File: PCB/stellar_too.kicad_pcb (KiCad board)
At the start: 2 copper layers, 139 x 121 mm, 61 parts, among them J1 USB_C_Receptacle_USB2.0_14P, J2 USB_C_Receptacle_USB2.0_16P, SW1 SW_Push_45deg, SW10 SW_Push_45deg, SW11 SW_Push_45deg, SW12 SW_Push_45deg, SW13 SW_Push_45deg, SW14 SW_Push_45deg, SW15 SW_Push_45deg, SW16 SW_Push_45deg, SW17 SW_Push_45deg, SW18 SW_Push_45deg, SW19 SW_Push_45deg, SW2 SW_Push_45deg, SW20 SW_Push_45deg, SW21 SW_Push_45deg, SW22 SW_Push_45deg, SW23 SW_Push_45deg, SW24 SW_Push_45deg, SW25 SW_Push_45deg, SW26 SW_Push_45deg, SW27 SW_Push_45deg, SW28 SW_Push_45deg, SW3 SW_Push_45deg, SW4 SW_Push_45deg, SW5 SW_Push_45deg, SW6 SW_Push_45deg, SW7 SW_Push_45deg, SW8 SW_Push_45deg, SW9 SW_Push_45deg, U1 MDBT50Q, U2 FUSB302B01MPX, U3 FUSB302B01MPX

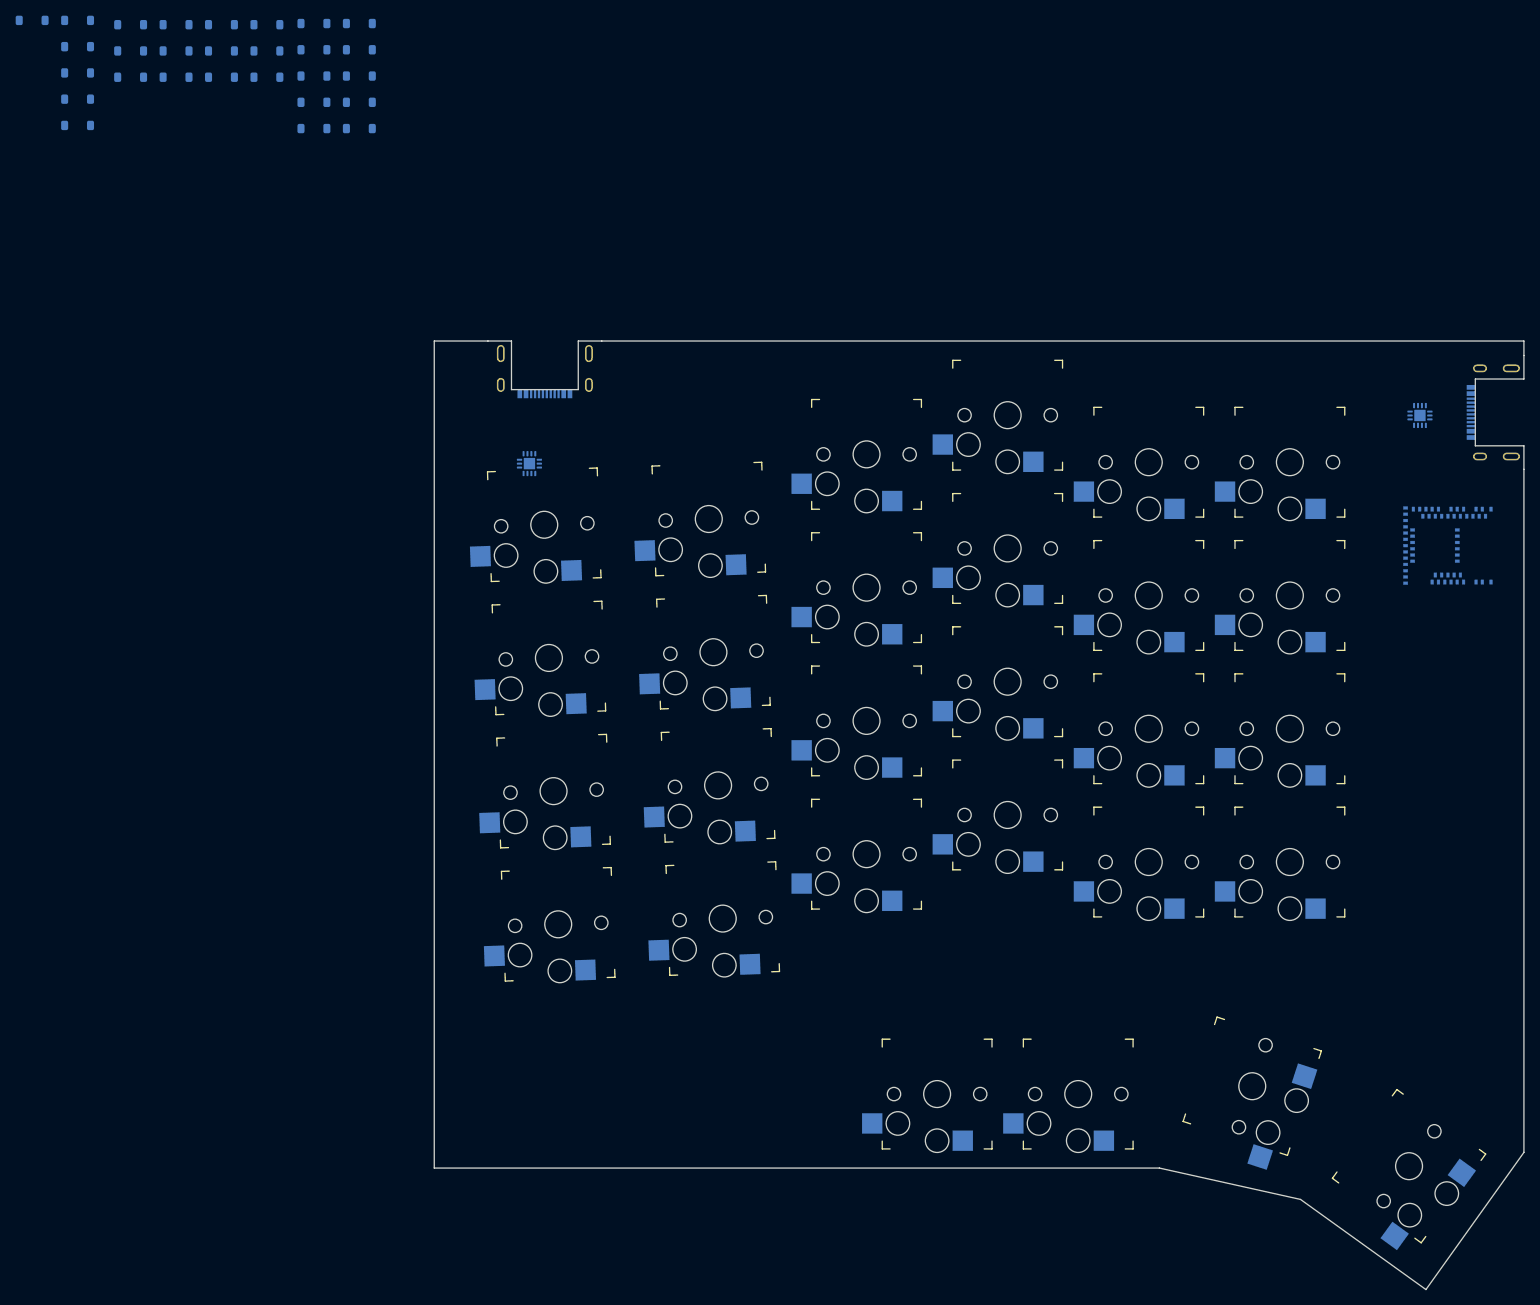
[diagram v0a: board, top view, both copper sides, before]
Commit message: feat(pcb) added e73-2g4m08s1c module
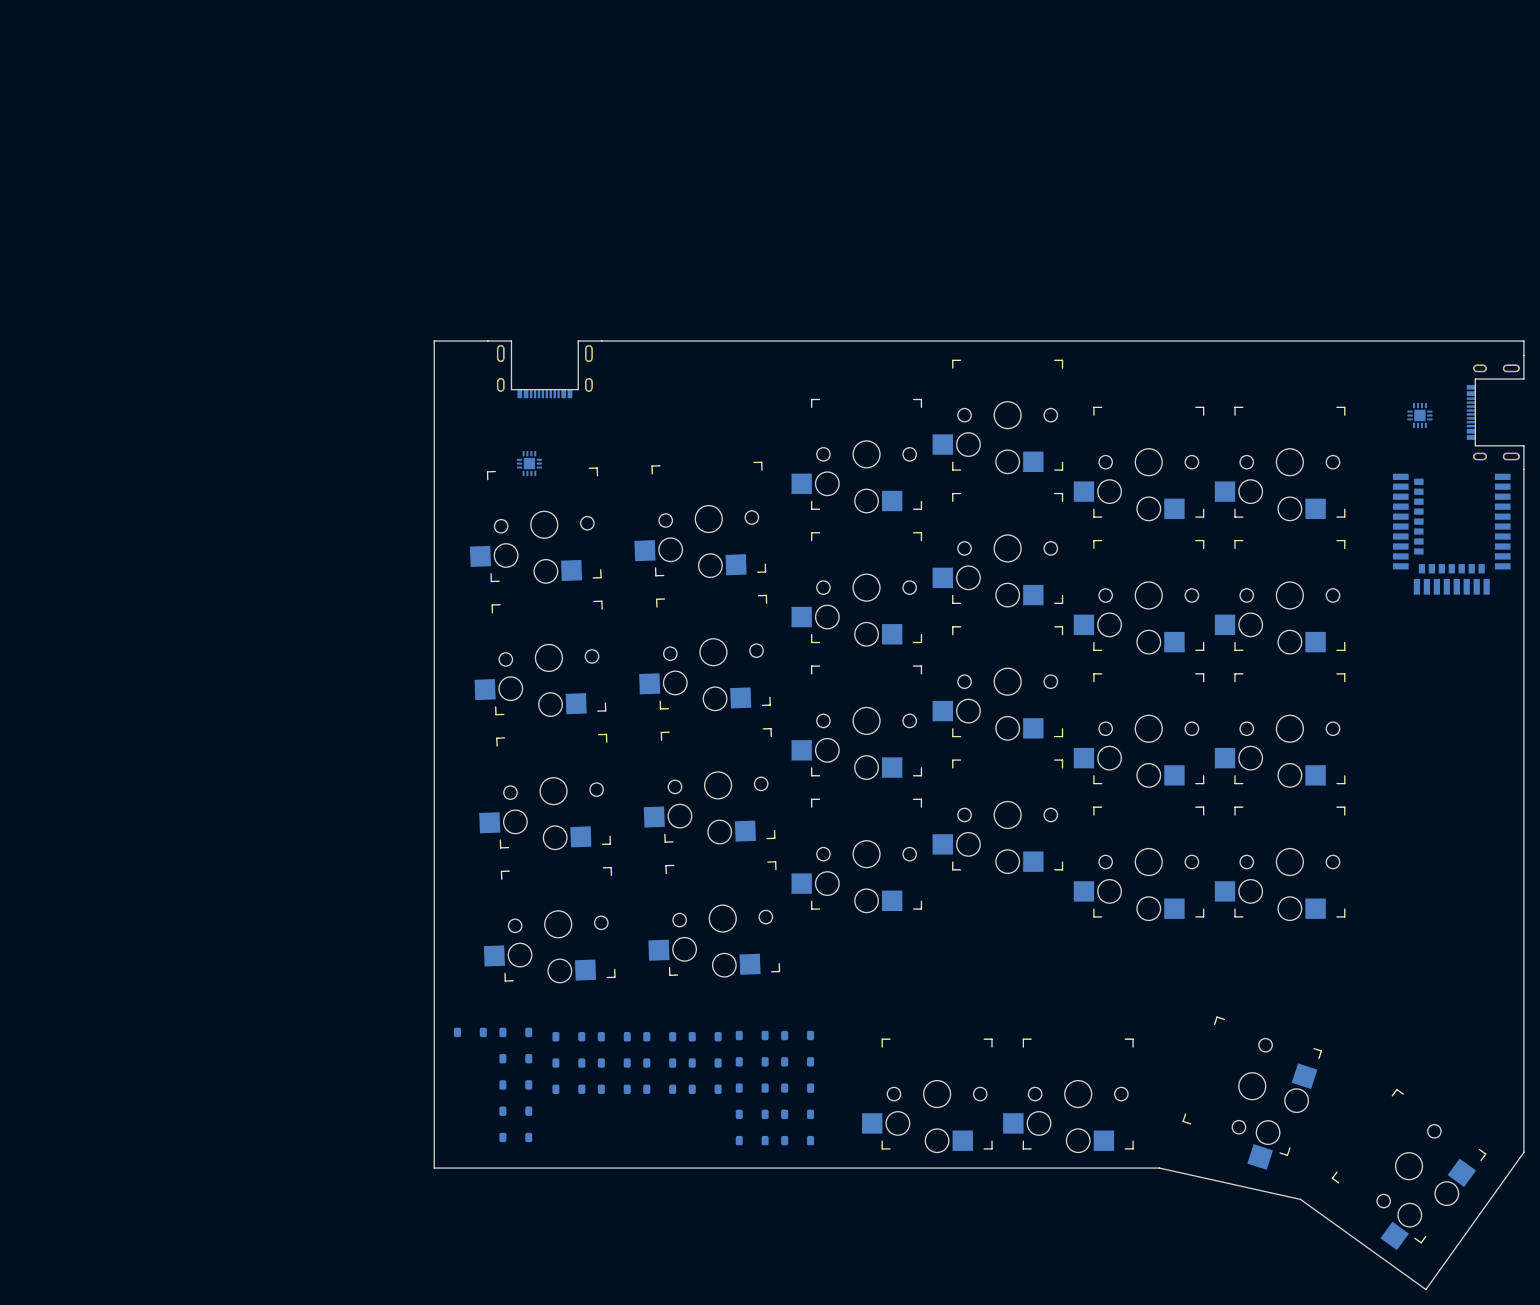
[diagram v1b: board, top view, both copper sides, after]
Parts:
- U1: value MDBT50Q -> E73(2G4M08S1C); footprint stellar:MDBT50Q -> stellar:E73(2G4M08S1C)
- moved D14 140.7 mm to (117.1, 128.3)
- moved D6 140.7 mm to (122.8, 128.3)
- moved D1 140.7 mm to (111.1, 121.8)
- moved D10 140.7 mm to (105.3, 125.1)
- moved D11 140.7 mm to (105.3, 128.4)
- moved D12 140.7 mm to (117.1, 121.6)
- moved D13 140.7 mm to (117.1, 125.0)
- moved D15 140.7 mm to (117.1, 131.7)
- moved D16 140.7 mm to (117.1, 135.0)
- moved D17 140.7 mm to (99.5, 121.8)
- moved D18 140.7 mm to (99.5, 125.1)
- moved D19 140.7 mm to (99.5, 128.4)
- moved D2 140.7 mm to (111.1, 125.1)
- moved D20 140.7 mm to (86.9, 121.2)
- moved D21 140.7 mm to (86.9, 124.5)
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
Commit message: feat(PCB) more wip
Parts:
- U1: footprint stellar:E73(2G4M08S1C) -> stellar:MDBT50Q
